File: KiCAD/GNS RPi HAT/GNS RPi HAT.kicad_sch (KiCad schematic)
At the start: 24 parts, among them J1 RPi_GPIO, J3 Conn_01x03_Pin, SW1 SW_DIP_x03, U2 CAT24C128, U3 PCF8574AT

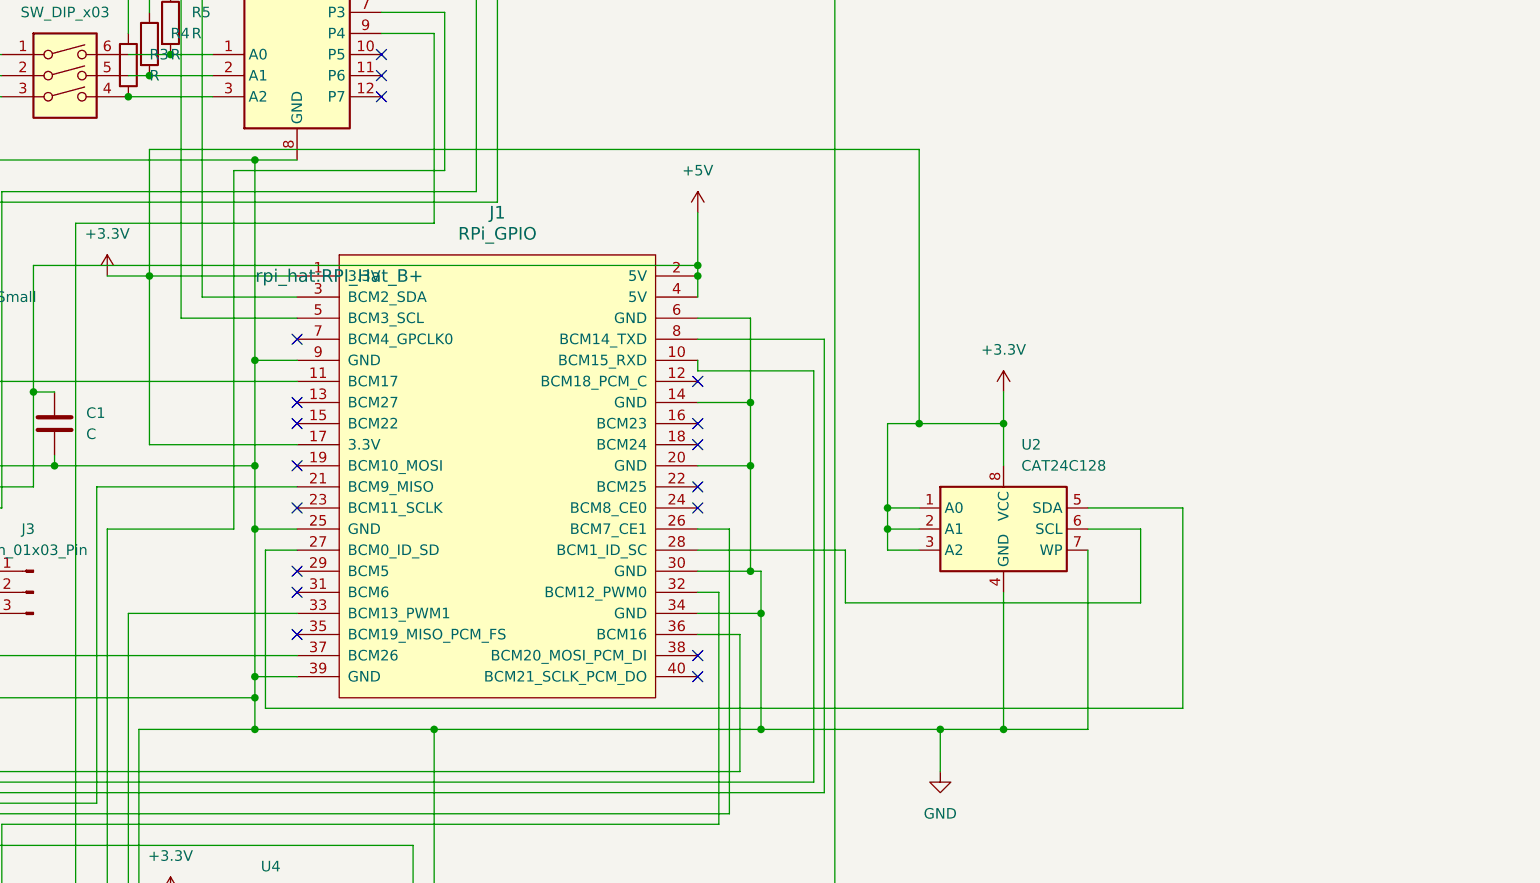
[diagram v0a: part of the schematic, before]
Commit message: Wechsel auf SMD-Bauteile, Fehlerkorrekturen
Die Widerstände und Leds wurden auf noch von Hand Lötbare SMD-Varianten geändert.
Die Platine wurde weiter aufgeräumt.
Wichtigste Änderung: die Adressierung des I2C Busses für die HAT+ Erkennung wurde von einer fixen Adresse auf Lötpads geändert.
Die Adressen 0x50, 0x51 und ggf. später weitere sind nun möglich um im Abhängigkeit zu anderen HAT keinen Adresskonflikt zu verursachen.
Das erste Design hatte noch fix die Adresse 0x5F, welcher in der Spec nicht automatisch erkannt wird.
Der Schreibschutz ist ebenfalls über eine Lötbrücke steuerbar.
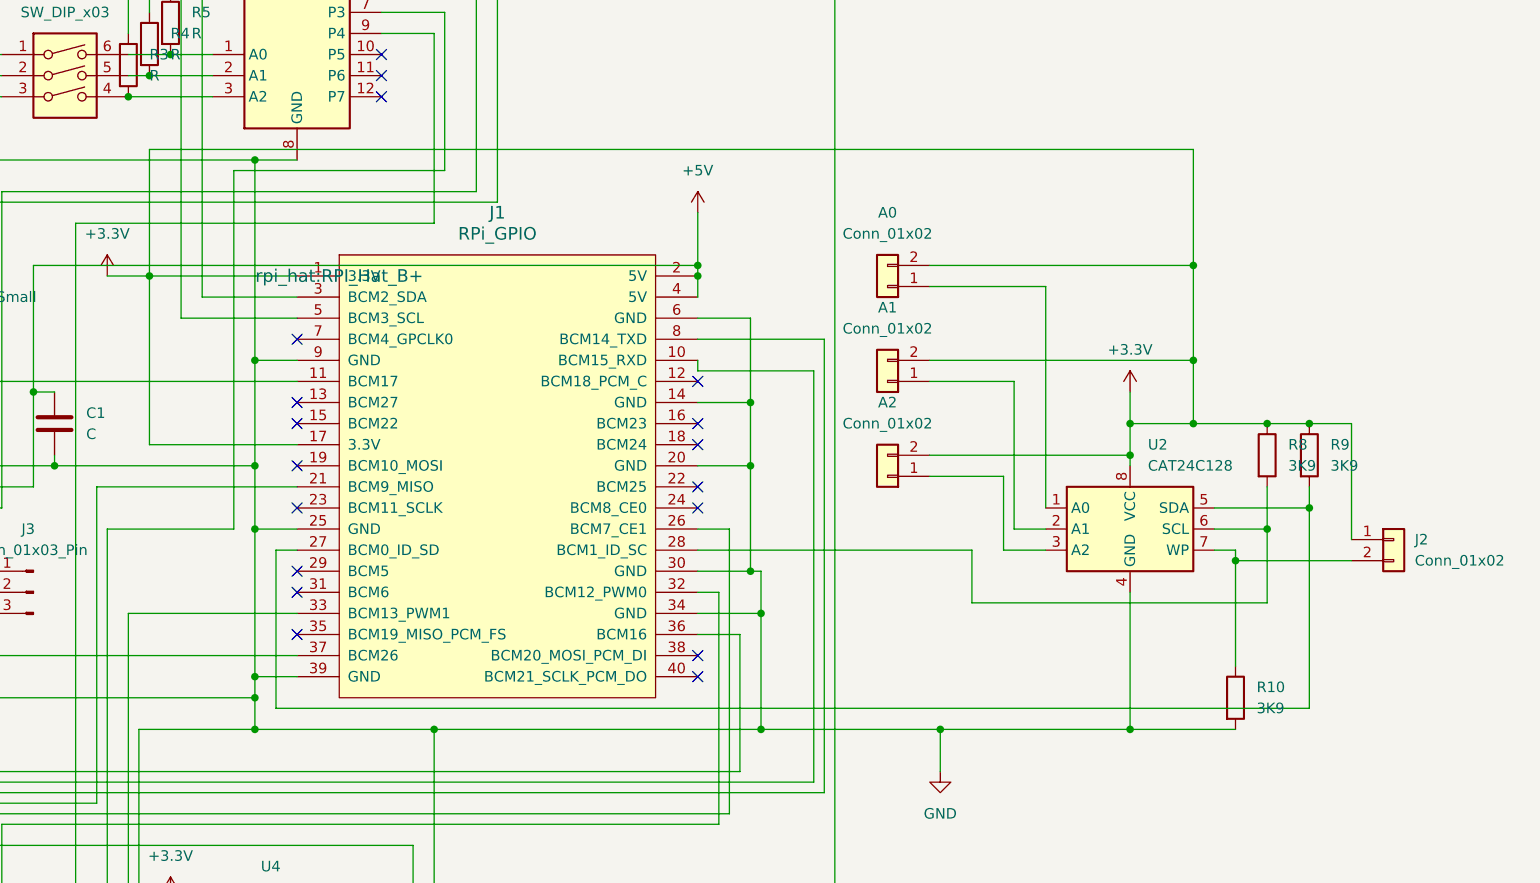
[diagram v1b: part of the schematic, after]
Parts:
- added A0, A1, A2: Conn_01x02, Jumper:SolderJumper-2_P1.3mm_Open_Pad1.0x1.5mm, symbol Connector_Generic:Conn_01x02
- added J2: Conn_01x02, Connector_PinSocket_2.54mm:PinSocket_1x02_P2.54mm_Vertical, symbol Connector_Generic:Conn_01x02
- added R10, R8, R9: 3K9, Resistor_SMD:R_0805_2012Metric_Pad1.20x1.40mm_HandSolder, symbol Device:R
- 3D-Fix1, ADSB-Frame1, AIS-Frame1, PPS1: footprint LED_THT:LED_D3.0mm -> LED_SMD:LED_0805_2012Metric_Pad1.15x1.40mm_HandSolder
- C1, C2, C3: footprint Capacitor_THT:C_Disc_D7.5mm_W2.5mm_P5.00mm -> Capacitor_SMD:C_0805_2012Metric_Pad1.18x1.45mm_HandSolder
- R1, R2, R3, R4, R5, R6, R7: footprint Resistor_THT:R_Axial_DIN0207_L6.3mm_D2.5mm_P5.08mm_Vertical -> Resistor_SMD:R_0805_2012Metric_Pad1.20x1.40mm_HandSolder
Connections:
- net +3.3V: now also A0.2 (Pin_2), A1.2 (Pin_2), A2.2 (Pin_2), J2.1 (Pin_1), R8.1, R9.1; no longer U2.1 (A0), U2.2 (A1), U2.3 (A2)
- net GND: now also R10.2; no longer U2.7 (WP)
- net at J1.27 (BCM0_ID_SD), U2.5 (SDA): now also R9.2
- net at J1.28 (BCM1_ID_SC), U2.6 (SCL): now also R8.2
- new net: A0.1 (Pin_1), U2.1 (A0)
- new net: A1.1 (Pin_1), U2.2 (A1)
- new net: A2.1 (Pin_1), U2.3 (A2)
- new net: J2.2 (Pin_2), R10.1, U2.7 (WP)
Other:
- moved on the sheet: U2
